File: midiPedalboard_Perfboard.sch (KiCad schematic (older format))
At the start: 49 parts, among them J1 wire, J10 wire, J11 wire, J12 wire, J13 wire, J14 wire, J15 MIDI_4, J16 MIDI_5, J17 MIDI_4, J18 MIDI_2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

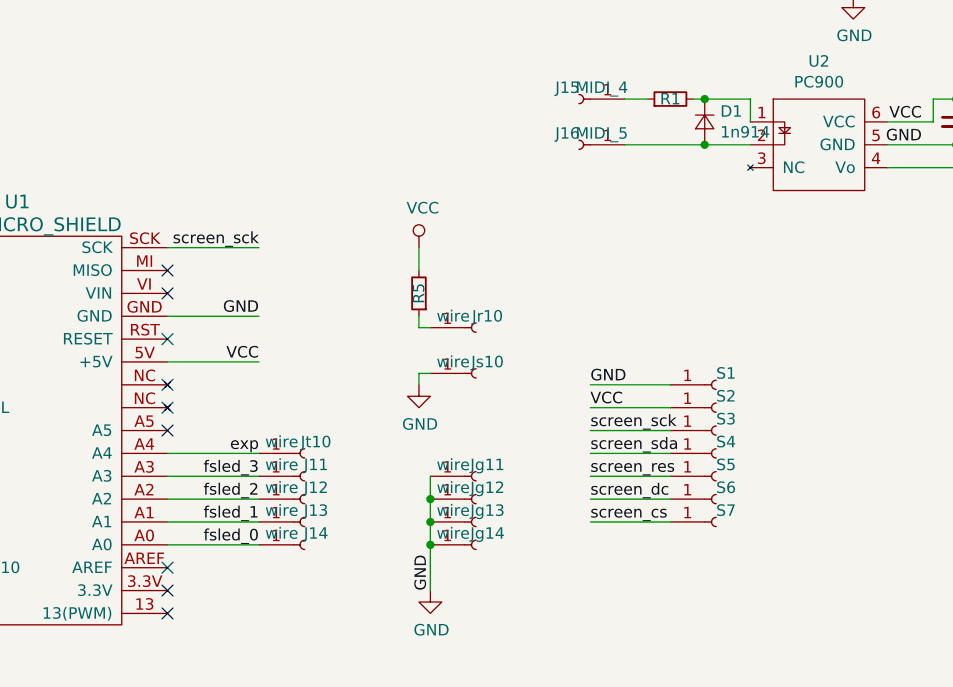
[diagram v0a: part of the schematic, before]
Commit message: add a second exp pedal input
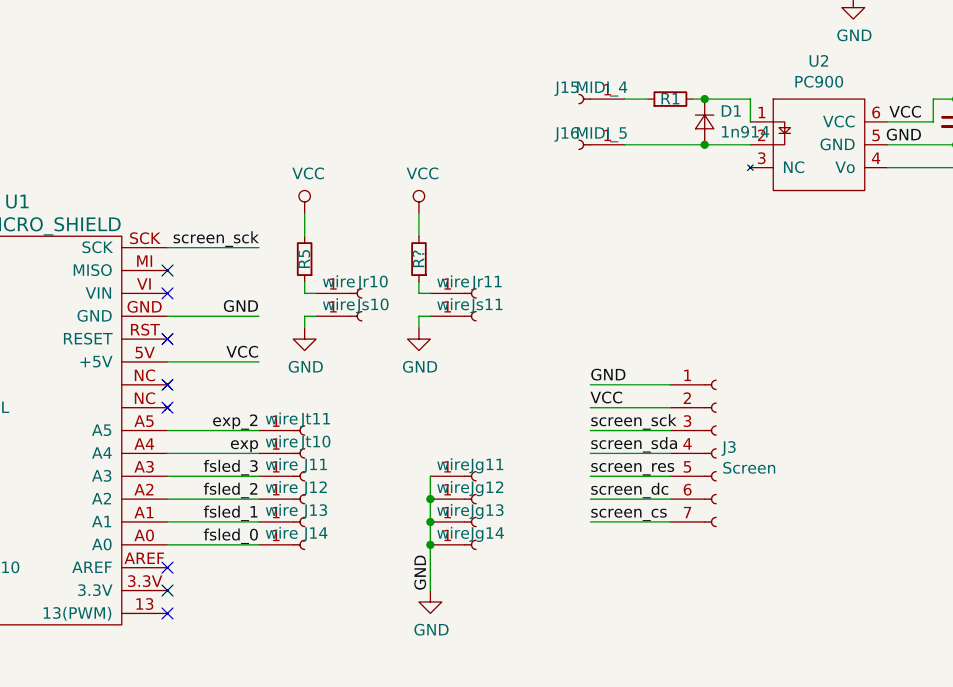
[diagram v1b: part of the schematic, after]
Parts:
- removed S1, S2, S3, S4, S5, S6, S7: Socket, Connector_PinSocket_2.54mm:PinSocket_1x01_P2.54mm_Horizontal, symbol Connector:Conn_01x01_Female
- added J3: Screen, Connector_PinSocket_2.54mm:PinSocket_1x07_P2.54mm_Horizontal, symbol Connector:Conn_01x07_Female
- added Jr11, Js11, Jt11: wire, Connector_Wire:SolderWirePad_1x01_Drill0.8mm, symbol Connector:Conn_01x01_Female
- added R?: 100, Resistor_THT:R_Axial_DIN0207_L6.3mm_D2.5mm_P2.54mm_Vertical, symbol Device:R_Small
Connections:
- net GND: now also J3.1 (Pin_1), Js11.1 (Pin_1)
- net VCC: now also J3.2 (Pin_2), R?.2
- net screen_cs: now also J3.7 (Pin_7)
- net screen_dc: now also J3.6 (Pin_6)
- net screen_res: now also J3.5 (Pin_5)
- net screen_sck: now also J3.3 (Pin_3)
- net screen_sda: now also J3.4 (Pin_4)
- net exp_2: now reaches U1.A5
- net exp_2: now also Jt11.1 (Pin_1)
- new net: Jr11.1 (Pin_1), R?.1
- no-connect marks 11 -> 10
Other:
- moved on the sheet: Jr10, Js10, R5
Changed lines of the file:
@@
 	-1   0    0    1
 $EndComp
-NoConn ~ 5900 3500
 NoConn ~ 5900 4100
 NoConn ~ 5900 4200
@@
 L Connector:Conn_01x01_Female Jr10
 U 1 1 5CAF6041
-P 7250 3050
-F 0 "Jr10" H 7300 3100 50  0000 C CNN
-F 1 "wire" H 7150 3100 50  0000 C CNN
-F 2 "Connector_Wire:SolderWirePad_1x01_Drill0.8mm" H 7250 3050 50  0001 C CNN
-F 3 "~" H 7250 3050 50  0001 C CNN
-	1    7250 3050
+P 6750 2900
+F 0 "Jr10" H 6800 2950 50  0000 C CNN
+F 1 "wire" H 6650 2950 50  0000 C CNN
+F 2 "Connector_Wire:SolderWirePad_1x01_Drill0.8mm" H 6750 2900 50  0001 C CNN
+F 3 "~" H 6750 2900 50  0001 C CNN
+	1    6750 2900
 	1    0    0    -1
 $EndComp
@@
 L Connector:Conn_01x01_Female Js10
 U 1 1 5CAF60E1
-P 7250 3250
-F 0 "Js10" H 7300 3300 50  0000 C CNN
-F 1 "wire" H 7150 3300 50  0000 C CNN
-F 2 "Connector_Wire:SolderWirePad_1x01_Drill0.8mm" H 7250 3250 50  0001 C CNN
-F 3 "~" H 7250 3250 50  0001 C CNN
-	1    7250 3250
+P 6750 3000
+F 0 "Js10" H 6800 3050 50  0000 C CNN
+F 1 "wire" H 6650 3050 50  0000 C CNN
+F 2 "Connector_Wire:SolderWirePad_1x01_Drill0.8mm" H 6750 3000 50  0001 C CNN
+F 3 "~" H 6750 3000 50  0001 C CNN
+	1    6750 3000
 	1    0    0    -1
 $EndComp
@@
 L Device:R_Small R5
 U 1 1 5CAF65EA
-P 7000 2900
-F 0 "R5" V 7000 2900 50  0000 C CNN
-F 1 "100" V 6895 2900 50  0001 C CNN
-F 2 "Resistor_THT:R_Axial_DIN0207_L6.3mm_D2.5mm_P2.54mm_Vertical" H 7000 2900 50  0001 C CNN
-F 3 "~" H 7000 2900 50  0001 C CNN
-	1    7000 2900
+P 6500 2750
+F 0 "R5" V 6500 2750 50  0000 C CNN
+F 1 "100" V 6395 2750 50  0001 C CNN
+F 2 "Resistor_THT:R_Axial_DIN0207_L6.3mm_D2.5mm_P2.54mm_Vertical" H 6500 2750 50  0001 C CNN
+F 3 "~" H 6500 2750 50  0001 C CNN
+	1    6500 2750
 	-1   0    0    1
 $EndComp
@@
 L power:VCC #PWR0109
 U 1 1 5CAF680A
-P 7000 2700
-F 0 "#PWR0109" H 7000 2550 50  0001 C CNN
-F 1 "VCC" H 7017 2873 50  0000 C CNN
-F 2 "" H 7000 2700 50  0001 C CNN
-F 3 "" H 7000 2700 50  0001 C CNN
-	1    7000 2700
-	1    0    0    -1
-$EndComp
-Wire Wire Line
-	7000 2700 7000 2800
-Wire Wire Line
-	7000 3000 7000 3050
-Wire Wire Line
-	7000 3050 7050 3050
-Wire Wire Line
-	7050 3250 7000 3250
-Wire Wire Line
-	7000 3250 7000 3300
+P 6500 2550
+F 0 "#PWR0109" H 6500 2400 50  0001 C CNN
+F 1 "VCC" H 6517 2723 50  0000 C CNN
+F 2 "" H 6500 2550 50  0001 C CNN
+F 3 "" H 6500 2550 50  0001 C CNN
+	1    6500 2550
+	1    0    0    -1
+$EndComp
+Wire Wire Line
+	6500 2550 6500 2650
+Wire Wire Line
+	6500 2850 6500 2900
+Wire Wire Line
+	6500 2900 6550 2900
+Wire Wire Line
+	6550 3000 6500 3000
+Wire Wire Line
+	6500 3000 6500 3050
 $Comp
 L power:GND #PWR0110
 U 1 1 5CAFA231
-P 7000 3300
-F 0 "#PWR0110" H 7000 3050 50  0001 C CNN
-F 1 "GND" H 7005 3127 50  0000 C CNN
-F 2 "" H 7000 3300 50  0001 C CNN
-F 3 "" H 7000 3300 50  0001 C CNN
-	1    7000 3300
+P 6500 3050
+F 0 "#PWR0110" H 6500 2800 50  0001 C CNN
+F 1 "GND" H 6505 2877 50  0000 C CNN
+F 2 "" H 6500 3050 50  0001 C CNN
+F 3 "" H 6500 3050 50  0001 C CNN
+	1    6500 3050
 	1    0    0    -1
 $EndComp
@@
 screen_cs
 $Comp
-L Connector:Conn_01x01_Female S1
-U 1 1 5CAE6698
-P 8300 3300
-F 0 "S1" H 8300 3350 50  0000 L CNN
-F 1 "Socket" H 8327 3235 50  0001 L CNN
-F 2 "Connector_PinSocket_2.54mm:PinSocket_1x01_P2.54mm_Horizontal" H 8300 3300 50  0001 C CNN
-F 3 "~" H 8300 3300 50  0001 C CNN
-	1    8300 3300
-	1    0    0    -1
-$EndComp
-$Comp
-L Connector:Conn_01x01_Female S2
-U 1 1 5CAE6A24
-P 8300 3400
-F 0 "S2" H 8300 3450 50  0000 L CNN
-F 1 "Socket" H 8327 3335 50  0001 L CNN
-F 2 "Connector_PinSocket_2.54mm:PinSocket_1x01_P2.54mm_Horizontal" H 8300 3400 50  0001 C CNN
-F 3 "~" H 8300 3400 50  0001 C CNN
-	1    8300 3400
-	1    0    0    -1
-$EndComp
-$Comp
-L Connector:Conn_01x01_Female S3
-U 1 1 5CAE6A92
-P 8300 3500
-F 0 "S3" H 8300 3550 50  0000 L CNN
-F 1 "Socket" H 8327 3435 50  0001 L CNN
-F 2 "Connector_PinSocket_2.54mm:PinSocket_1x01_P2.54mm_Horizontal" H 8300 3500 50  0001 C CNN
-F 3 "~" H 8300 3500 50  0001 C CNN
-	1    8300 3500
-	1    0    0    -1
-$EndComp
-$Comp
-L Connector:Conn_01x01_Female S4
-U 1 1 5CAE708E
+L Connector:Conn_01x07_Female J3
+U 1 1 5CCA11A5
 P 8300 3600
-F 0 "S4" H 8300 3650 50  0000 L CNN
-F 1 "Socket" H 8327 3535 50  0001 L CNN
-F 2 "Connector_PinSocket_2.54mm:PinSocket_1x01_P2.54mm_Horizontal" H 8300 3600 50  0001 C CNN
+F 0 "J3" H 8327 3626 50  0000 L CNN
+F 1 "Screen" H 8327 3535 50  0000 L CNN
+F 2 "Connector_PinSocket_2.54mm:PinSocket_1x07_P2.54mm_Horizontal" H 8300 3600 50  0001 C CNN
 F 3 "~" H 8300 3600 50  0001 C CNN
 	1    8300 3600
 	1    0    0    -1
 $EndComp
-$Comp
-L Connector:Conn_01x01_Female S5
-U 1 1 5CAE70FC
-P 8300 3700
-F 0 "S5" H 8300 3750 50  0000 L CNN
-F 1 "Socket" H 8327 3635 50  0001 L CNN
-F 2 "Connector_PinSocket_2.54mm:PinSocket_1x01_P2.54mm_Horizontal" H 8300 3700 50  0001 C CNN
-F 3 "~" H 8300 3700 50  0001 C CNN
-	1    8300 3700
-	1    0    0    -1
-$EndComp
-$Comp
-L Connector:Conn_01x01_Female S6
-U 1 1 5CAE7170
-P 8300 3800
-F 0 "S6" H 8300 3850 50  0000 L CNN
-F 1 "Socket" H 8327 3735 50  0001 L CNN
-F 2 "Connector_PinSocket_2.54mm:PinSocket_1x01_P2.54mm_Horizontal" H 8300 3800 50  0001 C CNN
-F 3 "~" H 8300 3800 50  0001 C CNN
-	1    8300 3800
-	1    0    0    -1
-$EndComp
-$Comp
-L Connector:Conn_01x01_Female S7
-U 1 1 5CAE71E2
-P 8300 3900
-F 0 "S7" H 8300 3950 50  0000 L CNN
-F 1 "Socket" H 8327 3835 50  0001 L CNN
-F 2 "Connector_PinSocket_2.54mm:PinSocket_1x01_P2.54mm_Horizontal" H 8300 3900 50  0001 C CNN
-F 3 "~" H 8300 3900 50  0001 C CNN
-	1    8300 3900
-	1    0    0    -1
-$EndComp
+Wire Wire Line
+	5900 3500 6300 3500
+Text Label 6300 3500 2    50   ~ 0
+exp_2
+$Comp
+L Connector:Conn_01x01_Female Jt11
+U 1 1 5CCAFC10
+P 6500 3500
+F 0 "Jt11" H 6550 3550 50  0000 C CNN
+F 1 "wire" H 6400 3550 50  0000 C CNN
+F 2 "Connector_Wire:SolderWirePad_1x01_Drill0.8mm" H 6500 3500 50  0001 C CNN
+F 3 "~" H 6500 3500 50  0001 C CNN
+	1    6500 3500
+	1    0    0    -1
+$EndComp
+$Comp
+L Connector:Conn_01x01_Female Jr11
+U 1 1 5CCBBBC1
+P 7250 2900
+F 0 "Jr11" H 7300 2950 50  0000 C CNN
+F 1 "wire" H 7150 2950 50  0000 C CNN
+F 2 "Connector_Wire:SolderWirePad_1x01_Drill0.8mm" H 7250 2900 50  0001 C CNN
+F 3 "~" H 7250 2900 50  0001 C CNN
+	1    7250 2900
+	1    0    0    -1
+$EndComp
+$Comp
+L Connector:Conn_01x01_Female Js11
+U 1 1 5CCBBBC8
+P 7250 3000
+F 0 "Js11" H 7300 3050 50  0000 C CNN
+F 1 "wire" H 7150 3050 50  0000 C CNN
+F 2 "Connector_Wire:SolderWirePad_1x01_Drill0.8mm" H 7250 3000 50  0001 C CNN
+F 3 "~" H 7250 3000 50  0001 C CNN
+	1    7250 3000
+	1    0    0    -1
+$EndComp
+$Comp
+L Device:R_Small R?
+U 1 1 5CCBBBCF
+P 7000 2750
+F 0 "R?" V 7000 2750 50  0000 C CNN
+F 1 "100" V 6895 2750 50  0001 C CNN
+F 2 "Resistor_THT:R_Axial_DIN0207_L6.3mm_D2.5mm_P2.54mm_Vertical" H 7000 2750 50  0001 C CNN
+F 3 "~" H 7000 2750 50  0001 C CNN
+	1    7000 2750
+	-1   0    0    1
+$EndComp
+$Comp
+L power:VCC #PWR?
+U 1 1 5CCBBBD6
+P 7000 2550
+F 0 "#PWR?" H 7000 2400 50  0001 C CNN
+F 1 "VCC" H 7017 2723 50  0000 C CNN
+F 2 "" H 7000 2550 50  0001 C CNN
+F 3 "" H 7000 2550 50  0001 C CNN
+	1    7000 2550
+	1    0    0    -1
+$EndComp
+Wire Wire Line
+	7000 2550 7000 2650
+Wire Wire Line
+	7000 2850 7000 2900
+Wire Wire Line
+	7000 2900 7050 2900
+Wire Wire Line
+	7050 3000 7000 3000
+Wire Wire Line
+	7000 3000 7000 3050
+$Comp
+L power:GND #PWR?
+U 1 1 5CCBBBE1
+P 7000 3050
+F 0 "#PWR?" H 7000 2800 50  0001 C CNN
+F 1 "GND" H 7005 2877 50  0000 C CNN
+F 2 "" H 7000 3050 50  0001 C CNN
+F 3 "" H 7000 3050 50  0001 C CNN
+	1    7000 3050
+	1    0    0    -1
+$EndComp

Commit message: some placment and connection
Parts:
- gave numbers to parts that had none: 1
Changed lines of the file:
@@
 $EndComp
 $Comp
-L Device:R_Small R?
+L Device:R_Small R6
 U 1 1 5CCBBBCF
 P 7000 2750
-F 0 "R?" V 7000 2750 50  0000 C CNN
+F 0 "R6" V 7000 2750 50  0000 C CNN
 F 1 "100" V 6895 2750 50  0001 C CNN
 F 2 "Resistor_THT:R_Axial_DIN0207_L6.3mm_D2.5mm_P2.54mm_Vertical" H 7000 2750 50  0001 C CNN
@@
 $EndComp
 $Comp
-L power:VCC #PWR?
+L power:VCC #PWR0101
 U 1 1 5CCBBBD6
 P 7000 2550
-F 0 "#PWR?" H 7000 2400 50  0001 C CNN
+F 0 "#PWR0101" H 7000 2400 50  0001 C CNN
 F 1 "VCC" H 7017 2723 50  0000 C CNN
 F 2 "" H 7000 2550 50  0001 C CNN
@@
 	7000 3000 7000 3050
 $Comp
-L power:GND #PWR?
+L power:GND #PWR0111
 U 1 1 5CCBBBE1
 P 7000 3050
-F 0 "#PWR?" H 7000 2800 50  0001 C CNN
+F 0 "#PWR0111" H 7000 2800 50  0001 C CNN
 F 1 "GND" H 7005 2877 50  0000 C CNN
 F 2 "" H 7000 3050 50  0001 C CNN

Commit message: relayout and connection
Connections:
- net btn_cancel: now also U1.6 (6(PWM)/A7); no longer U1.8 (8/A8)
- net btn_ok: now also U1.5 (5(PWM)); no longer U1.7
- net rotary_a: now also U1.7; no longer U1.2 (2/SDA)
- net rotary_b: now also U1.8 (8/A8); no longer U1.3 (3(PWM)/SCL)
- net screen_dc: now also U1.3 (3(PWM)/SCL); no longer U1.5 (5(PWM))
- net screen_res: now also U1.2 (2/SDA); no longer U1.6 (6(PWM)/A7)
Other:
- moved on the sheet: J6, J7
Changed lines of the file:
@@
 	1    0    0    -1
 $EndComp
-Text Label 4150 3300 0    50   ~ 0
+Text Label 4150 3800 0    50   ~ 0
 rotary_a
-Text Label 4150 3400 0    50   ~ 0
+Text Label 4150 3900 0    50   ~ 0
 rotary_b
 Text Label 4150 3500 0    50   ~ 0
 screen_cs
 Wire Wire Line
-	4150 3300 4550 3300
+	4150 3800 4550 3800
+Wire Wire Line
+	4150 3900 4550 3900
+Wire Wire Line
+	4150 3500 4550 3500
 Wire Wire Line
 	4150 3400 4550 3400
 Wire Wire Line
-	4150 3500 4550 3500
+	4150 3300 4550 3300
 Wire Wire Line
 	4150 3600 4550 3600
 Wire Wire Line
 	4150 3700 4550 3700
-Wire Wire Line
-	4150 3800 4550 3800
-Wire Wire Line
-	4150 3900 4550 3900
 Wire Wire Line
 	4150 4000 4550 4000
@@
 Wire Wire Line
 	4150 4300 4550 4300
+Text Label 4150 3400 0    50   ~ 0
+screen_dc
+Text Label 4150 3300 0    50   ~ 0
+screen_res
 Text Label 4150 3600 0    50   ~ 0
-screen_dc
+btn_ok
 Text Label 4150 3700 0    50   ~ 0
-screen_res
-Text Label 4150 3800 0    50   ~ 0
-btn_ok
-Text Label 4150 3900 0    50   ~ 0
 btn_cancel
 Text Label 4150 4000 0    50   ~ 0
@@
 L Connector:Conn_01x01_Female J6
 U 1 1 5CABD334
-P 3950 3800
-F 0 "J6" H 4000 3750 50  0000 C CNN
-F 1 "wire" H 3850 3750 50  0000 C CNN
-F 2 "Connector_Wire:SolderWirePad_1x01_Drill0.8mm" H 3950 3800 50  0001 C CNN
-F 3 "~" H 3950 3800 50  0001 C CNN
-	1    3950 3800
+P 3950 3600
+F 0 "J6" H 4000 3550 50  0000 C CNN
+F 1 "wire" H 3850 3550 50  0000 C CNN
+F 2 "Connector_Wire:SolderWirePad_1x01_Drill0.8mm" H 3950 3600 50  0001 C CNN
+F 3 "~" H 3950 3600 50  0001 C CNN
+	1    3950 3600
 	-1   0    0    1
 $EndComp
@@
 L Connector:Conn_01x01_Female J7
 U 1 1 5CABD51F
-P 3950 3900
-F 0 "J7" H 4000 3850 50  0000 C CNN
-F 1 "wire" H 3850 3850 50  0000 C CNN
-F 2 "Connector_Wire:SolderWirePad_1x01_Drill0.8mm" H 3950 3900 50  0001 C CNN
-F 3 "~" H 3950 3900 50  0001 C CNN
-	1    3950 3900
+P 3950 3700
+F 0 "J7" H 4000 3650 50  0000 C CNN
+F 1 "wire" H 3850 3650 50  0000 C CNN
+F 2 "Connector_Wire:SolderWirePad_1x01_Drill0.8mm" H 3950 3700 50  0001 C CNN
+F 3 "~" H 3950 3700 50  0001 C CNN
+	1    3950 3700
 	-1   0    0    1
 $EndComp
